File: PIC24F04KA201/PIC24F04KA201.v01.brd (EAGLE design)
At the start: 160 x 100 mm, 27 parts, among them IC2 3V3-APE1117K-33-HF-3, IC3 3V3-APE1117K-33-HF-3

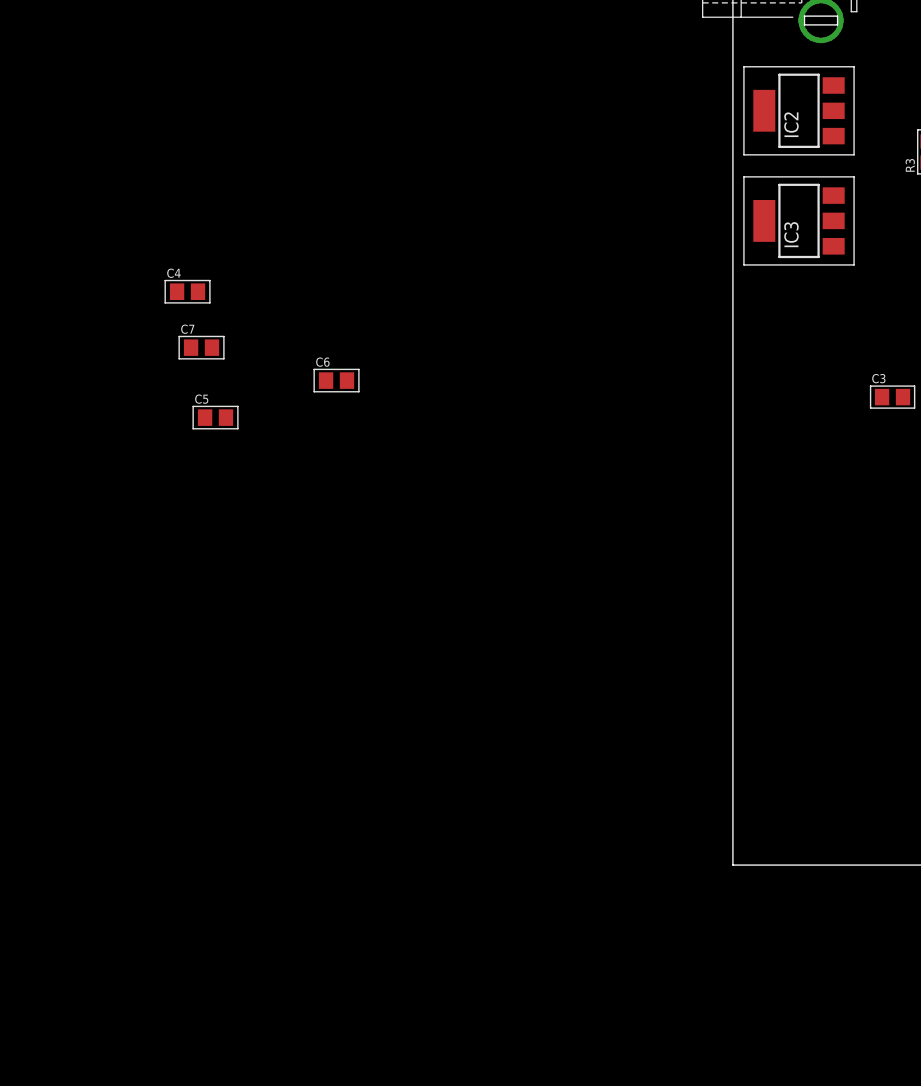
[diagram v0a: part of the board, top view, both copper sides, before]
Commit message: Update - added jumpers & Vreg's
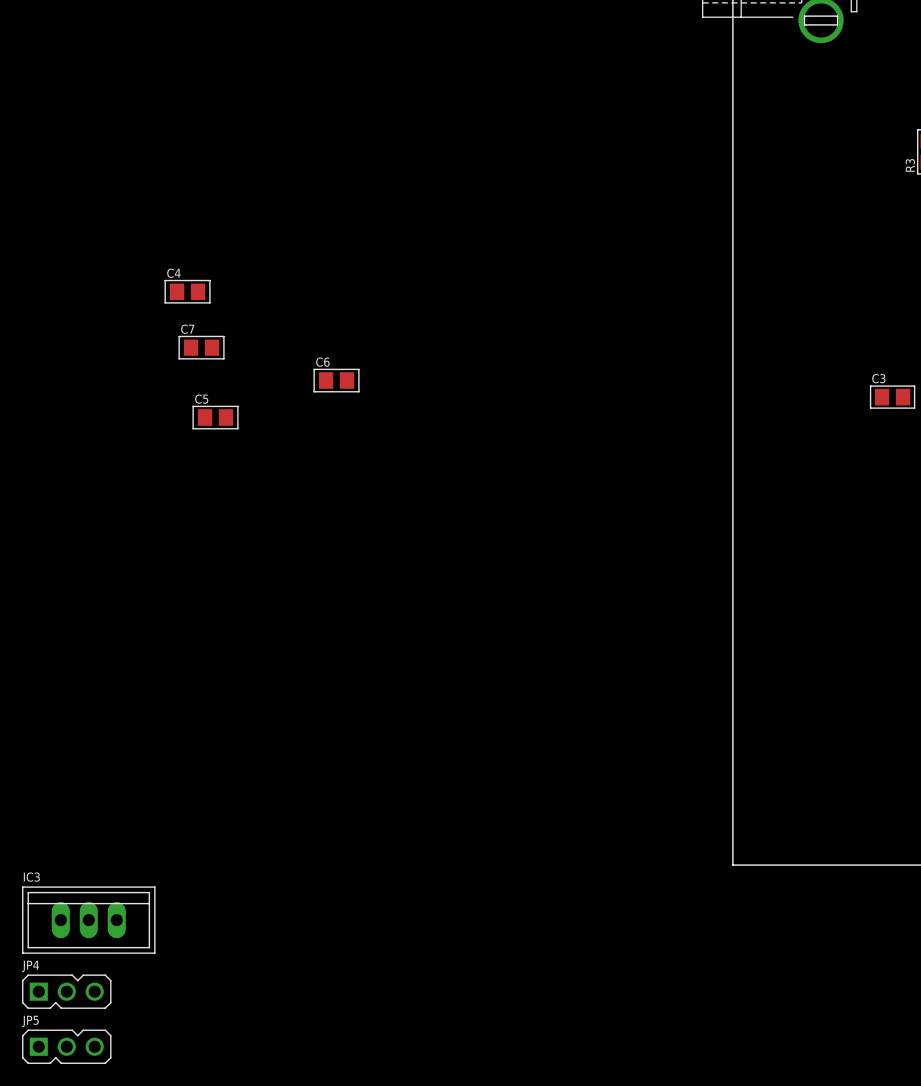
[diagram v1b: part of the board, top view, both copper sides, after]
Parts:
- removed IC2: 3V3-APE1117K-33-HF-3, SM-VReg:SOT223
- added JP4, JP5: (no value), SM-Jumper:1X3
- IC3: value 3V3-APE1117K-33-HF-3 -> (none); device SM-VReg:SOT223 -> SM-VReg:TO-220-STANDING
- moved IC3 90.5 mm to (-58.5, -5.00), turned to 0 degrees
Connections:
- removed net N$2: IC1.2, JP2.2
- removed net N$20: IC1.9, JP3.1
- removed net N$21: IC1.10, JP3.2
- removed net N$3: IC1.3, JP2.3
- new net PGC2: IC1.2, JP2.2, JP4.1
- new net PGC3: IC1.10, JP3.2, JP4.3
- new net PGD: JP5.2
- new net PGD2: IC1.3, JP2.3, JP5.1
- new net PGD3: IC1.9, JP3.1, JP5.3
- net +12V: no longer IC2.3
- net +3V3: now also IC3.2; no longer IC2.4
- net +5V: no longer IC3.4
- net GND: no longer IC2.1
- net PGC: now also JP4.2
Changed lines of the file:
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@@
 <element name="C7" library="SM-Capacitors" package="SMD-0805@1" value="" x="-48.26" y="46.99"/>
 <element name="ISCP1" library="SM-Microchip" package="1X6-2.54" value="ICSP1X6-2.54" x="33.5" y="18.5" rot="R270"/>
-<element name="IC2" library="SM-VReg" package="SOT223" value="3V3-APE1117K-33-HF-3" x="6" y="68.5" rot="R90"/>
 <element name="C2" library="SM-Capacitors" package="SMD-0805" value="" x="33.02" y="93.98"/>
 <element name="C8" library="SM-Capacitors" package="SMD-0805" value="" x="38.1" y="76.2"/>
@@
 <element name="R4" library="SM-Resistor" package="SMD-0805" value="" x="24.13" y="72.39"/>
 <element name="R5" library="SM-Resistor" package="SMD-0805" value="" x="28.5" y="62" rot="R90"/>
-<element name="IC3" library="SM-VReg" package="SOT223" value="3V3-APE1117K-33-HF-3" x="6" y="58.5" rot="R90"/>
 <element name="C9" library="SM-Capacitors" package="SMD-0805" value="" x="58.5" y="68"/>
 <element name="C10" library="SM-Capacitors" package="SMD-0805" value="" x="48" y="65"/>
@@
 <element name="JP3" library="SM-PinHeader" package="1X8" value="" x="55.5" y="47.5" rot="R180"/>
 <element name="CN1" library="SM-PinHeader" package="1X2" value="" x="42.5" y="47.5" rot="R180"/>
+<element name="IC3" library="SM-VReg" package="TO-220-STANDING" value="" x="-58.5" y="-5">
+<attribute name="PACKAGE" value="TO-220" x="-58.5" y="-5" size="1.778" layer="27" display="off"/>
+<attribute name="CURRENT" value="0.8 A" x="-58.5" y="-5" size="1.778" layer="27" display="off"/>
+<attribute name="VIN-MIN" value="4.5V" x="-58.5" y="-5" size="1.778" layer="27" display="off"/>
+<attribute name="MANUFACTURER" value="ST Microelectronics" x="-58.5" y="-5" size="1.778" layer="27" display="off"/>
+<attribute name="TME" value="LD1117V33" x="-58.5" y="-5" size="1.778" layer="27" display="off"/>
+<attribute name="VIN-MAX" value="15 V" x="-58.5" y="-5" size="1.778" layer="27" display="off"/>
+<attribute name="VOUT" value="3.3 V" x="-58.5" y="-5" size="1.778" layer="27" display="off"/>
+</element>
+<element name="JP4" library="SM-Jumper" package="1X3" value="" x="-60.5" y="-11"/>
+<element name="JP5" library="SM-Jumper" package="1X3" value="" x="-60.5" y="-16"/>
 </elements>
 <signals>
@@
 <contactref element="ISCP1" pad="2"/>
 <contactref element="C3" pad="2"/>
-<contactref element="IC2" pad="4"/>
 <contactref element="C2" pad="2"/>
 <contactref element="LED2" pad="A"/>
-<wire x1="33.97" y1="93.98" x2="24.45" y2="93.98" width="0" layer="19" extent="1-1"/>
-<wire x1="2.85" y1="68.5" x2="33.97" y2="93.98" width="0" layer="19" extent="1-1"/>
-<wire x1="27.05" y1="42.5" x2="2.85" y2="68.5" width="0" layer="19" extent="1-1"/>
+<contactref element="IC3" pad="2"/>
+<wire x1="24.45" y1="93.98" x2="33.97" y2="93.98" width="0" layer="19" extent="1-1"/>
+<wire x1="27.05" y1="42.5" x2="24.45" y2="93.98" width="0" layer="19" extent="1-1"/>
 <wire x1="15.45" y1="42.5" x2="27.05" y2="42.5" width="0" layer="19" extent="1-1"/>
-<wire x1="34" y1="22.31" x2="15.45" y2="42.5" width="0" layer="19" extent="1-1"/>
+<wire x1="34" y1="22.31" x2="27.05" y2="42.5" width="0" layer="19" extent="1-1"/>
+<wire x1="-58.5" y1="-5" x2="15.45" y2="42.5" width="0" layer="19" extent="1-1"/>
 </signal>
 <signal name="GND">
 <contactref element="ISCP1" pad="3"/>
 <contactref element="C3" pad="1"/>
-<contactref element="IC2" pad="1"/>
 <contactref element="C8" pad="1"/>
 <contactref element="C2" pad="1"/>
@@
 <contactref element="R4" pad="1"/>
 <contactref element="R5" pad="1"/>
-<contactref element="IC3" pad="1"/>
 <contactref element="C10" pad="1"/>
 <contactref element="C9" pad="1"/>
 <contactref element="C1" pad="1"/>
-<wire x1="9.15" y1="56.2" x2="22.55" y2="30" width="0" layer="19" extent="1-1"/>
-<wire x1="57.55" y1="68" x2="9.15" y2="56.2" width="0" layer="19" extent="1-1"/>
-<wire x1="47.05" y1="65" x2="57.55" y2="68" width="0" layer="19" extent="1-1"/>
-<wire x1="28.5" y1="61.05" x2="9.15" y2="56.2" width="0" layer="19" extent="1-1"/>
-<wire x1="23.18" y1="72.39" x2="28.5" y2="61.05" width="0" layer="19" extent="1-1"/>
+<contactref element="IC3" pad="1"/>
+<wire x1="37.15" y1="76.2" x2="32.07" y2="93.98" width="0" layer="19" extent="1-1"/>
+<wire x1="23.18" y1="72.39" x2="37.15" y2="76.2" width="0" layer="19" extent="1-1"/>
 <wire x1="17.78" y1="63.82" x2="23.18" y2="72.39" width="0" layer="19" extent="1-1"/>
-<wire x1="37.15" y1="76.2" x2="17.78" y2="63.82" width="0" layer="19" extent="1-1"/>
-<wire x1="32.07" y1="93.98" x2="37.15" y2="76.2" width="0" layer="19" extent="1-1"/>
-<wire x1="9.15" y1="66.2" x2="32.07" y2="93.98" width="0" layer="19" extent="1-1"/>
-<wire x1="5" y1="81.5" x2="9.15" y2="66.2" width="0" layer="19" extent="1-1"/>
-<wire x1="13.55" y1="42.5" x2="9.15" y2="66.2" width="0" layer="19" extent="1-1"/>
-<wire x1="34" y1="19.77" x2="13.55" y2="42.5" width="0" layer="19" extent="1-1"/>
+<wire x1="28.5" y1="61.05" x2="17.78" y2="63.82" width="0" layer="19" extent="1-1"/>
+<wire x1="47.05" y1="65" x2="37.15" y2="76.2" width="0" layer="19" extent="1-1"/>
+<wire x1="57.55" y1="68" x2="47.05" y2="65" width="0" layer="19" extent="1-1"/>
+<wire x1="5" y1="81.5" x2="23.18" y2="72.39" width="0" layer="19" extent="1-1"/>
+<wire x1="13.55" y1="42.5" x2="17.78" y2="63.82" width="0" layer="19" extent="1-1"/>
+<wire x1="22.55" y1="30" x2="13.55" y2="42.5" width="0" layer="19" extent="1-1"/>
+<wire x1="34" y1="19.77" x2="22.55" y2="30" width="0" layer="19" extent="1-1"/>
+<wire x1="-61.04" y1="-5" x2="13.55" y2="42.5" width="0" layer="19" extent="1-1"/>
 </signal>
 <signal name="MCLR">
@@
 <signal name="PGC">
 <contactref element="ISCP1" pad="5"/>
+<contactref element="JP4" pad="2"/>
+<wire x1="34" y1="14.69" x2="-60.5" y2="-11.5" width="0" layer="19" extent="1-1"/>
 </signal>
 <signal name="+12V">
-<contactref element="IC2" pad="3"/>
 <contactref element="C8" pad="2"/>
 <contactref element="J1" pad="3"/>
 <contactref element="LED1" pad="A"/>
+<contactref element="C10" pad="2"/>
 <contactref element="IC3" pad="3"/>
-<contactref element="C10" pad="2"/>
-<wire x1="9.15" y1="60.8" x2="48.95" y2="65" width="0" layer="19" extent="1-1"/>
+<wire x1="48.95" y1="65" x2="39.05" y2="76.2" width="0" layer="19" extent="1-1"/>
 <wire x1="33.5" y1="60.55" x2="48.95" y2="65" width="0" layer="19" extent="1-1"/>
-<wire x1="39.05" y1="76.2" x2="33.5" y2="60.55" width="0" layer="19" extent="1-1"/>
-<wire x1="9.15" y1="70.8" x2="39.05" y2="76.2" width="0" layer="19" extent="1-1"/>
-<wire x1="11" y1="81.5" x2="9.15" y2="70.8" width="0" layer="19" extent="1-1"/>
+<wire x1="11" y1="81.5" x2="39.05" y2="76.2" width="0" layer="19" extent="1-1"/>
+<wire x1="-55.96" y1="-5" x2="11" y2="81.5" width="0" layer="19" extent="1-1"/>
 </signal>
 <signal name="N$5">
@@
 </signal>
 <signal name="+5V">
-<contactref element="IC3" pad="4"/>
 <contactref element="C9" pad="2"/>
 <contactref element="LED3" pad="A"/>
-<wire x1="2.85" y1="58.5" x2="59.45" y2="68" width="0" layer="19" extent="1-1"/>
-<wire x1="54.93" y1="90.17" x2="2.85" y2="58.5" width="0" layer="19" extent="1-1"/>
+<wire x1="59.45" y1="68" x2="54.93" y2="90.17" width="0" layer="19" extent="1-1"/>
 </signal>
 <signal name="N$1">
@@
 <wire x1="24" y1="20" x2="24.45" y2="30" width="0" layer="19" extent="1-1"/>
 </signal>
-<signal name="N$2">
-<contactref element="IC1" pad="2"/>
-<contactref element="JP2" pad="2"/>
-<wire x1="39.11" y1="35.19" x2="44.42" y2="29.5" width="0" layer="19" extent="1-1"/>
-</signal>
-<signal name="N$3">
-<contactref element="IC1" pad="3"/>
-<contactref element="JP2" pad="3"/>
-<wire x1="41.65" y1="35.19" x2="46.96" y2="29.5" width="0" layer="19" extent="1-1"/>
-</signal>
 <signal name="N$4">
 <contactref element="IC1" pad="4"/>
@@
 <wire x1="41.65" y1="42.81" x2="41.25" y2="47.5" width="0" layer="19" extent="1-1"/>
 </signal>
-<signal name="N$20">
-<contactref element="JP3" pad="1"/>
-<contactref element="IC1" pad="9"/>
-<wire x1="56.89" y1="35.19" x2="64.62" y2="47.5" width="0" layer="19" extent="1-1"/>
-</signal>
-<signal name="N$21">
-<contactref element="JP3" pad="2"/>
-<contactref element="IC1" pad="10"/>
-<wire x1="59.43" y1="35.19" x2="62.08" y2="47.5" width="0" layer="19" extent="1-1"/>
-</signal>
 <signal name="RPIN">
 <contactref element="IC1" pad="1"/>
@@
 <wire x1="30.45" y1="26.5" x2="36.57" y2="35.19" width="0" layer="19" extent="1-1"/>
 </signal>
+<signal name="PGC3">
+<contactref element="JP4" pad="3"/>
+<contactref element="JP3" pad="2"/>
+<contactref element="IC1" pad="10"/>
+<wire x1="59.43" y1="35.19" x2="62.08" y2="47.5" width="0" layer="19" extent="1-1"/>
+<wire x1="-57.96" y1="-11.5" x2="59.43" y2="35.19" width="0" layer="19" extent="1-1"/>
+</signal>
+<signal name="PGD2">
+<contactref element="JP5" pad="1"/>
+<contactref element="IC1" pad="3"/>
+<contactref element="JP2" pad="3"/>
+<wire x1="41.65" y1="35.19" x2="-63.04" y2="-16.5" width="0" layer="19" extent="1-1"/>
+<wire x1="46.96" y1="29.5" x2="41.65" y2="35.19" width="0" layer="19" extent="1-1"/>
+</signal>
+<signal name="PGD">
+<contactref element="JP5" pad="2"/>
+</signal>
+<signal name="PGD3">
+<contactref element="JP5" pad="3"/>
+<contactref element="JP3" pad="1"/>
+<contactref element="IC1" pad="9"/>
+<wire x1="56.89" y1="35.19" x2="64.62" y2="47.5" width="0" layer="19" extent="1-1"/>
+<wire x1="-57.96" y1="-16.5" x2="56.89" y2="35.19" width="0" layer="19" extent="1-1"/>
+</signal>
+<signal name="PGC2">
+<contactref element="JP4" pad="1"/>
+<contactref element="IC1" pad="2"/>
+<contactref element="JP2" pad="2"/>
+<wire x1="39.11" y1="35.19" x2="-63.04" y2="-11.5" width="0" layer="19" extent="1-1"/>
+<wire x1="44.42" y1="29.5" x2="39.11" y2="35.19" width="0" layer="19" extent="1-1"/>
+</signal>
 </signals>

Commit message: Small parts update
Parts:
- moved JP5 116.1 mm to (53.0, 8.50)
- moved JP4 115.7 mm to (53.0, 11.5)
- moved IC3 100.8 mm to (12.0, 67.0), turned to 90 degrees
- moved R1 6.40 mm to (34.5, 30.5)
- moved JP2 6.10 mm to (46.0, 26.0)
- moved ISCP1 3.20 mm to (31.5, 16.0)
- moved JP1 3.00 mm to (21.0, 20.0)
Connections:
- removed net PGD: JP5.2
- net PDG: now also JP5.2

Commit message: Added correct values for resistors, resynced the board file
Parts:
- removed C4, C5, C6, C7: (no value), SM-Capacitors:SMD-0805@1
- added IC2: (no value), SM-VReg:TO-220-STANDING
- R1: value (none) -> 1 kΩ; device SM-Resistor:SMD-0805 -> SM-Resistor:SMD-2012(0805)
- R2: value (none) -> 10 kΩ; device SM-Resistor:SMD-0805 -> SM-Resistor:SMD-2012(0805)
- R3: value (none) -> 680 Ω; device SM-Resistor:SMD-0805 -> SM-Resistor:SMD-2012(0805)
- R4: value (none) -> 270 Ω; device SM-Resistor:SMD-0805 -> SM-Resistor:SMD-2012(0805)
- R5: value (none) -> 2.2 kΩ; device SM-Resistor:SMD-0805 -> SM-Resistor:SMD-2012(0805)
- moved IC3 26.2 mm to (9.00, 41.0)
- moved IC1 2.83 mm to (50.0, 37.0)
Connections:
- net +12V: now also IC2.3, IC3.1; no longer IC3.3
- net +3V3: now also IC1.20, IC2.2; no longer IC3.2
- net +5V: now also IC3.3
- net GND: now also IC1.19, IC2.1, IC3.2; no longer IC3.1

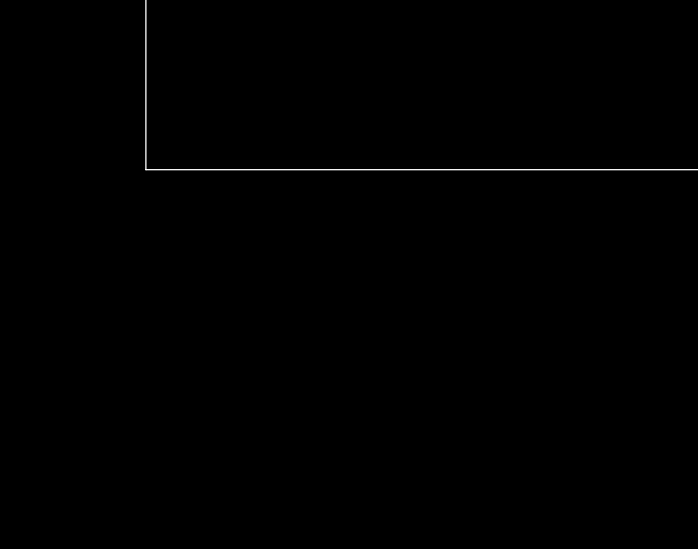
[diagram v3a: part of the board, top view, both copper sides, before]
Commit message: Added dip8
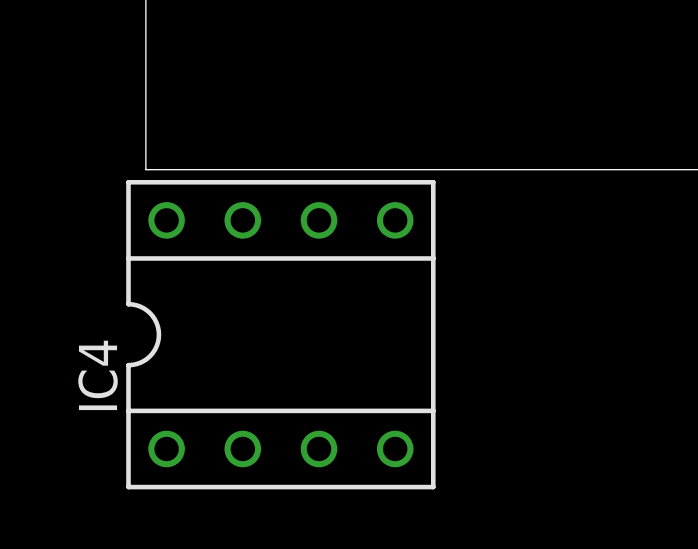
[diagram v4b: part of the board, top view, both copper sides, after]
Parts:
- added IC4: (no value), SM-IC-Packages:DIP-08-SOCKET
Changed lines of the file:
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@@
 <attribute name="VOUT" value="5.0 V" x="9" y="41" size="1.778" layer="27" rot="R90" display="off"/>
 </element>
+<element name="IC4" library="SM-IC-Packages" package="DIP-08-SOCKET" value="" x="4.5" y="-5.5"/>
 </elements>
 <signals>
